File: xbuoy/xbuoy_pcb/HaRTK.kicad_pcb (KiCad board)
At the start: 4 copper layers, 65 x 40 mm, 23 parts, among them J5 Gen, U1 RaspberryPi, U2 TLV70233_SOT23-5, U3 RFM22B, U4 NV08C-CSM

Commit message: Finished board
Signed-off-by: hardiepienaar <hardiepienaar@gmail.com>
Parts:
- added G***: LOGO, Images:skimage, F.Cu at (124.8, 88.2)
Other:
- board text added: "Spray it, dont say it"

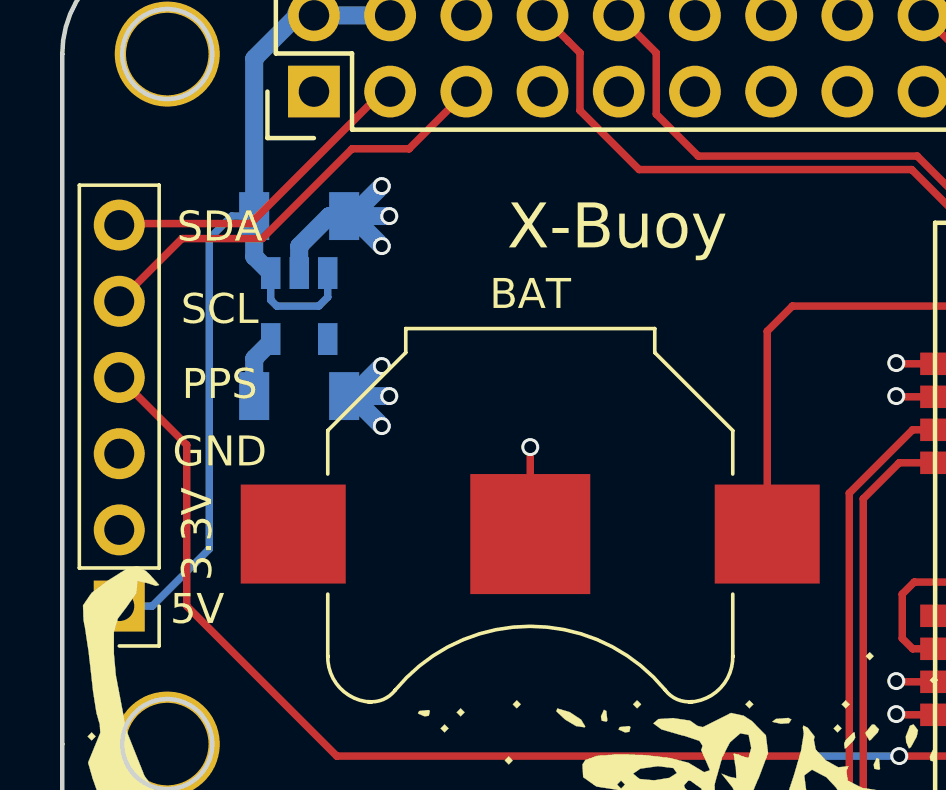
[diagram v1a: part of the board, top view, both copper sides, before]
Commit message: Fixed 3.3V rail disconnect, sht
Signed-off-by: hardiepienaar <hardiepienaar@gmail.com>
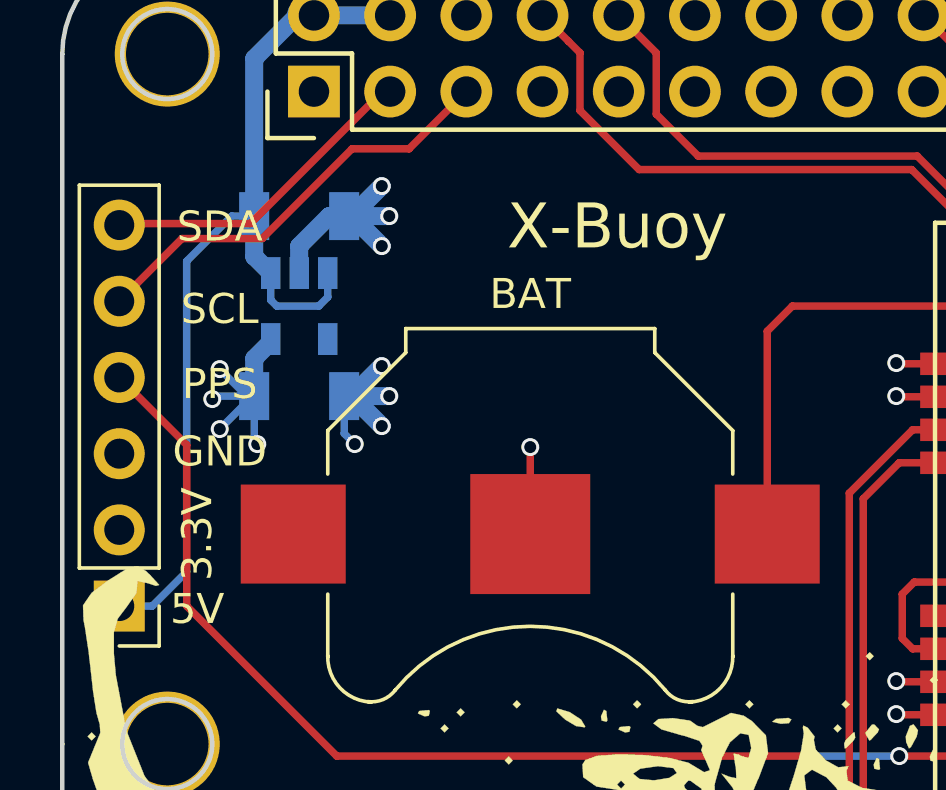
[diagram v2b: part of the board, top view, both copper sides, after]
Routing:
- net +3V3: track 14.1 -> 20.3 mm, vias 7 -> 11
- net GND: track 66.1 -> 67.9 mm, vias 35 -> 36
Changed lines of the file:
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@@
     (thickness 1.6)
     (drawings 47)
-    (tracks 339)
+    (tracks 354)
     (zones 0)
     (modules 24)
@@
     (effects (font (size 1.5 1.5) (thickness 0.3)) (justify mirror))
   )
-  (gr_text X-Buoy (at 128.5 69.25 360) (layer F.SilkS)
+  (gr_text X-Buoy (at 128.5 69.25) (layer F.SilkS)
     (effects (font (size 1.5 1.5) (thickness 0.3)))
   )
@@
   (gr_line (start 113.5 63.5) (end 113.5 60) (layer Dwgs.User) (width 0.2))
   (gr_line (start 142.5 60) (end 142.5 55) (layer Dwgs.User) (width 0.2))
-  (segment (start 114.9 69.65) (end 114.9 80) (width 0.25) (layer B.Cu) (net 1))
-  (segment (start 114.9 80) (end 113 81.9) (width 0.25) (layer B.Cu) (net 1))
+  (segment (start 116.4 68.9) (end 115.65 68.9) (width 0.25) (layer B.Cu) (net 1))
+  (segment (start 115.65 68.9) (end 114.147318 70.402682) (width 0.25) (layer B.Cu) (net 1))
+  (segment (start 114.147318 70.402682) (end 114.147318 80.752682) (width 0.25) (layer B.Cu) (net 1))
+  (segment (start 114.147318 80.752682) (end 113 81.9) (width 0.25) (layer B.Cu) (net 1))
   (segment (start 113 81.9) (end 111.9 81.9) (width 0.25) (layer B.Cu) (net 1))
-  (segment (start 116.4 68.9) (end 115.65 68.9) (width 0.25) (layer B.Cu) (net 1))
-  (segment (start 115.65 68.9) (end 114.9 69.65) (width 0.25) (layer B.Cu) (net 1))
   (segment (start 118.85 70.8) (end 118.85 71.6) (width 0.25) (layer B.Cu) (net 1))
   (segment (start 116.95 71.7) (end 116.95 70.8) (width 0.25) (layer B.Cu) (net 1))
@@
   (segment (start 117.9 62.15) (end 116.4 63.65) (width 0.6) (layer B.Cu) (net 1))
   (segment (start 116.4 63.65) (end 116.4 68.9) (width 0.6) (layer B.Cu) (net 1))
+  (segment (start 119.4 74.9) (end 119.4 76.15) (width 0.25) (layer B.Cu) (net 2))
+  (segment (start 119.4 76.15) (end 119.75 76.5) (width 0.25) (layer B.Cu) (net 2))
+  (via (at 119.75 76.5) (size 0.6) (drill 0.4) (layers F.Cu B.Cu) (net 2))
   (segment (start 112.25 93.25) (end 112.25 94.5) (width 0.25) (layer F.Cu) (net 2))
   (segment (start 112.25 94.5) (end 112.4 94.65) (width 0.25) (layer F.Cu) (net 2))
@@
   (segment (start 119.4 68.9) (end 120.9 68.9) (width 0.6) (layer B.Cu) (net 2))
   (via (at 120.9 68.9) (size 0.6) (drill 0.4) (layers F.Cu B.Cu) (net 2))
+  (segment (start 116.4 74.9) (end 116.4 76.4) (width 0.25) (layer B.Cu) (net 3))
+  (segment (start 116.4 76.4) (end 116.5 76.5) (width 0.25) (layer B.Cu) (net 3))
+  (via (at 116.5 76.5) (size 0.6) (drill 0.4) (layers F.Cu B.Cu) (net 3))
+  (segment (start 116.4 74.9) (end 116.15 74.9) (width 0.25) (layer B.Cu) (net 3))
+  (segment (start 116.15 74.9) (end 115.25 74) (width 0.25) (layer B.Cu) (net 3))
+  (via (at 115.25 74) (size 0.6) (drill 0.4) (layers F.Cu B.Cu) (net 3))
+  (segment (start 116.4 74.9) (end 116.35 74.9) (width 0.25) (layer B.Cu) (net 3))
+  (segment (start 116.35 74.9) (end 115.25 76) (width 0.25) (layer B.Cu) (net 3))
+  (via (at 115.25 76) (size 0.6) (drill 0.4) (layers F.Cu B.Cu) (net 3))
+  (segment (start 116.4 74.9) (end 115.1 74.9) (width 0.25) (layer B.Cu) (net 3))
+  (segment (start 115.1 74.9) (end 115 75) (width 0.25) (layer B.Cu) (net 3))
+  (via (at 115 75) (size 0.6) (drill 0.4) (layers F.Cu B.Cu) (net 3))
   (segment (start 115.5 93) (end 115.5 94) (width 0.25) (layer F.Cu) (net 3))
   (via (at 115.65 94.15) (size 0.6) (drill 0.4) (layers F.Cu B.Cu) (net 3))
